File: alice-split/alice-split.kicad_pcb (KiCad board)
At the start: 2 copper layers, 434.2 x 120 mm, 214 parts, among them J1 MJ-4PP-9-Lily58-cache-Lily58_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, J2 OLED-Lily58-cache, J3 OLED-Lily58-cache, J4 MJ-4PP-9-Lily58-cache-Lily58_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, SW38 SW_PUSH-MX_W_LED, SW39 SW_PUSH-MX_W_LED, SW40 SW_PUSH-MX_W_LED, SW41 SW_PUSH-MX_W_LED, SW42 SW_PUSH-MX_W_LED, SW43 SW_PUSH-MX_W_LED, SW44 SW_PUSH-MX_W_LED, SW45 SW_PUSH-MX_W_LED, SW46 SW_PUSH-MX_W_LED, SW47 SW_PUSH-MX_W_LED, SW48 SW_PUSH-MX_W_LED, SW49 SW_PUSH-MX_W_LED, SW50 SW_PUSH-MX_W_LED, SW51 SW_PUSH-MX_W_LED, SW52 SW_PUSH-MX_W_LED, SW53 SW_PUSH-MX_W_LED, SW54 SW_PUSH-MX_W_LED, SW55 SW_PUSH-MX_W_LED, SW56 SW_PUSH-MX_W_LED, SW57 SW_PUSH-MX_W_LED, SW58 SW_PUSH-MX_W_LED, SW59 SW_PUSH-MX_W_LED, SW60 SW_PUSH-MX_W_LED, SW61 SW_PUSH-MX_W_LED, SW62 SW_PUSH-MX_W_LED, SW63 SW_PUSH-MX_W_LED, SW64 SW_PUSH-MX_W_LED, SW65 SW_PUSH-MX_W_LED, SW66 SW_PUSH-MX_W_LED, SW67 SW_PUSH-MX_W_LED, SW68 SW_PUSH-MX_W_LED, SW69 SW_PUSH-MX_W_LED, SW70 SW_PUSH-MX_W_LED, SW71 SW_PUSH-MX_W_LED, SW72 SW_PUSH-MX_W_LED, SW73 SW_PUSH-MX_W_LED, SW74 SW_PUSH-MX_W_LED, SW75 SW_PUSH-MX_W_LED, SW76 SW_PUSH-MX_W_LED, SW77 SW_PUSH-MX_W_LED, SW78 SW_PUSH-MX_W_LED, SW79 SW_PUSH-MX_W_LED, SW80 SW_PUSH-MX_W_LED, SW81 SW_PUSH-MX_W_LED, SW82 SW_PUSH-MX_W_LED, SW83 SW_PUSH-MX_W_LED, SW84 SW_PUSH-MX_W_LED, SW85 SW_PUSH-MX_W_LED, SW86 SW_PUSH-MX_W_LED, SW87 SW_PUSH-MX_W_LED, SW88 SW_PUSH-MX_W_LED, SW89 SW_PUSH-MX_W_LED, U1 Sparkfun_Pro_Micro, U2 ProMicro_2-Lily58-cache-Lily5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

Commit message: Working on making the outer profiles of the PCBs more consistent with each other design wise.
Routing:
- net GND: track 2924.6 -> 2939.3 mm
- net /Right Hand Side/COL0: track 281.2 -> 282.0 mm
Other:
- outline, holes or cut-outs redrawn

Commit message: Started trying to re-arrange the left hand side macro keys.
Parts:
- added D40: D_Small, Diode_SMD:D_1206_3216Metric, B.Cu at (49.2, 134.5)
- added D74: D_Small, Diode_SMD:D_1206_3216Metric, B.Cu at (48.5, 111.5)
- added R3: R_Small, SofleKeyboard-footprint:R_1206_DoubleSided, F.Cu at (292.1, 68.5)
- added R4: R_Small, SofleKeyboard-footprint:R_1206_DoubleSided, F.Cu at (292.1, 71.8)
- added SW_MACRO3: SW_PUSH-MX_W_LED, SofleRGB:SK6812MINI_and_cherry, F.Cu at (56.5, 109.9)
- added SW_MACRO4: SW_PUSH-MX_W_LED, SofleRGB:SK6812MINI_and_cherry, F.Cu at (463.7, 124.8)
- moved SW_MACRO2 406.6 mm to (57.1, 132.9)
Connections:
- SW_MACRO2 pad 1: Net-(SW_MACRO2B-DOUT) -> unconnected-(SW_MACRO2B-DOUT-Pad1)
- SW_MACRO2 pad 2: /Right Hand Side/VCC -> unconnected-(SW_MACRO2B-VSS-Pad2)
- SW_MACRO2 pad 3: Net-(D_ENC_R1-DOUT) -> unconnected-(SW_MACRO2B-DIN-Pad3)
- SW_MACRO2 pad 4: GND -> unconnected-(SW_MACRO2B-VDD-Pad4)
- SW_MACRO2 pad 5: Net-(D73-A) -> Net-(D40-A)
- SW_MACRO2 pad 6: /Right Hand Side/COL1 -> /COL6
- SW_MOD_R1 pad 3: Net-(SW_MACRO2B-DOUT) -> Net-(SW_MACRO4B-DOUT)
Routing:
- net Net-(SW_MACRO4B-DOUT): track 0.00 -> 89.0 mm
- net Net-(SW_MACRO2B-DOUT): track 89.0 -> 0.00 mm
- net /ROW2: track 234.6 -> 224.5 mm
- net /ROW1: track 246.8 -> 237.7 mm
- net Net-(SW_MACRO1B-DOUT): track 162.7 -> 160.3 mm
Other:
- board size 434.2 x 120 mm -> 434.2 x 119.2 mm

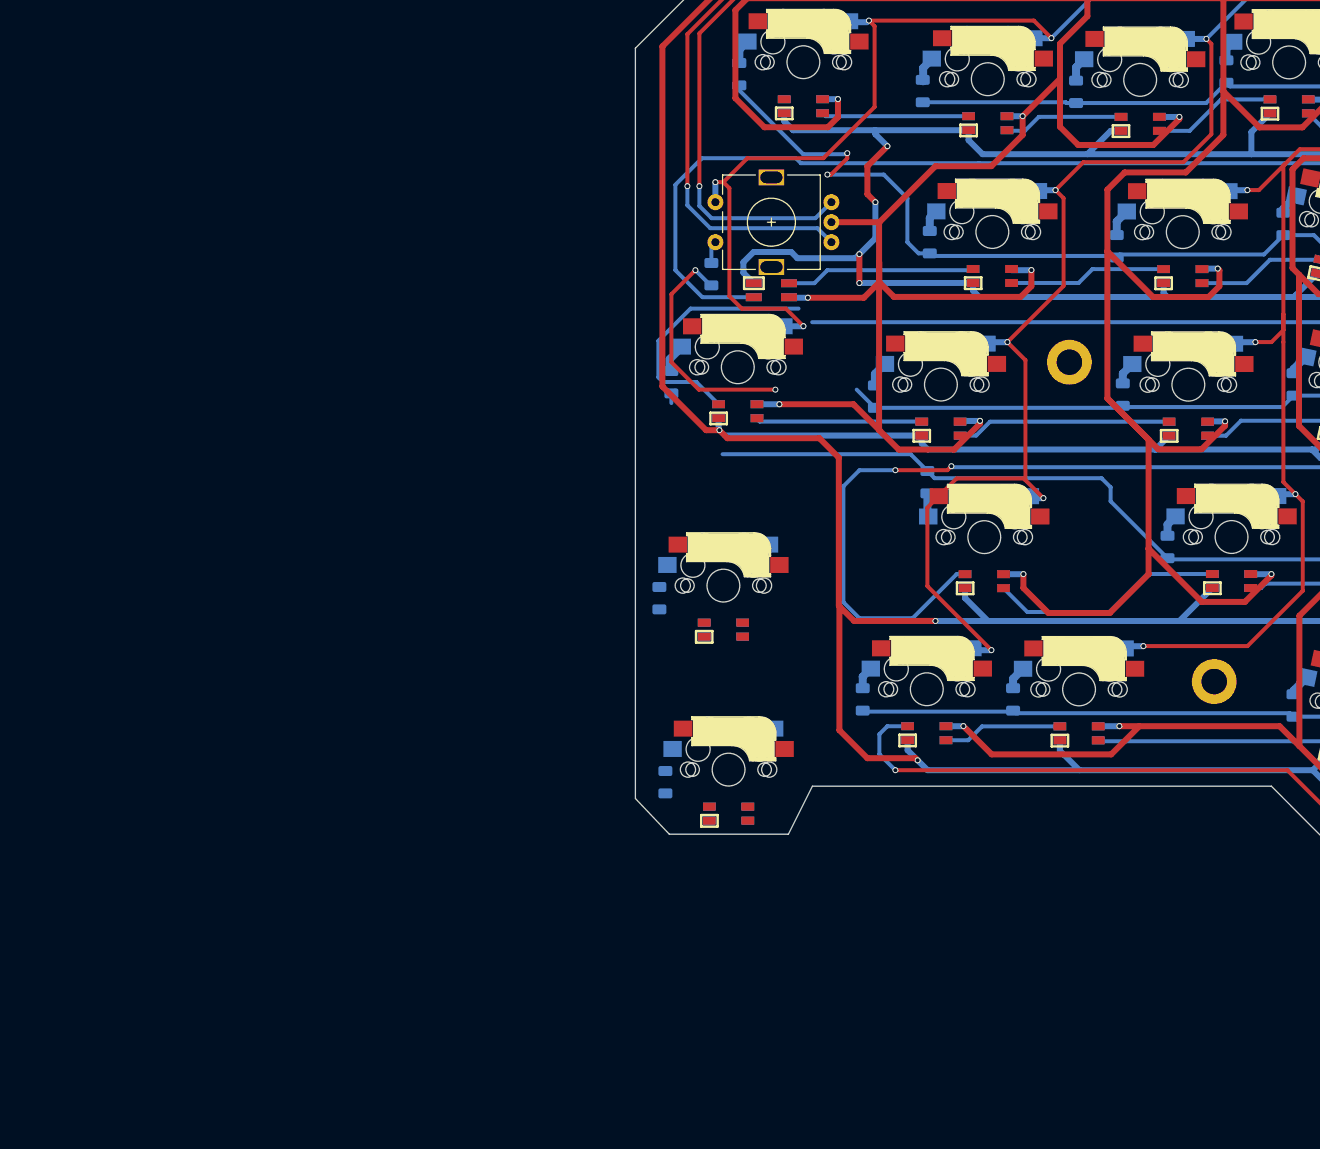
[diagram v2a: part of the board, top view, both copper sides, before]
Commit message: Working on adding more macro keys to the left hand side.
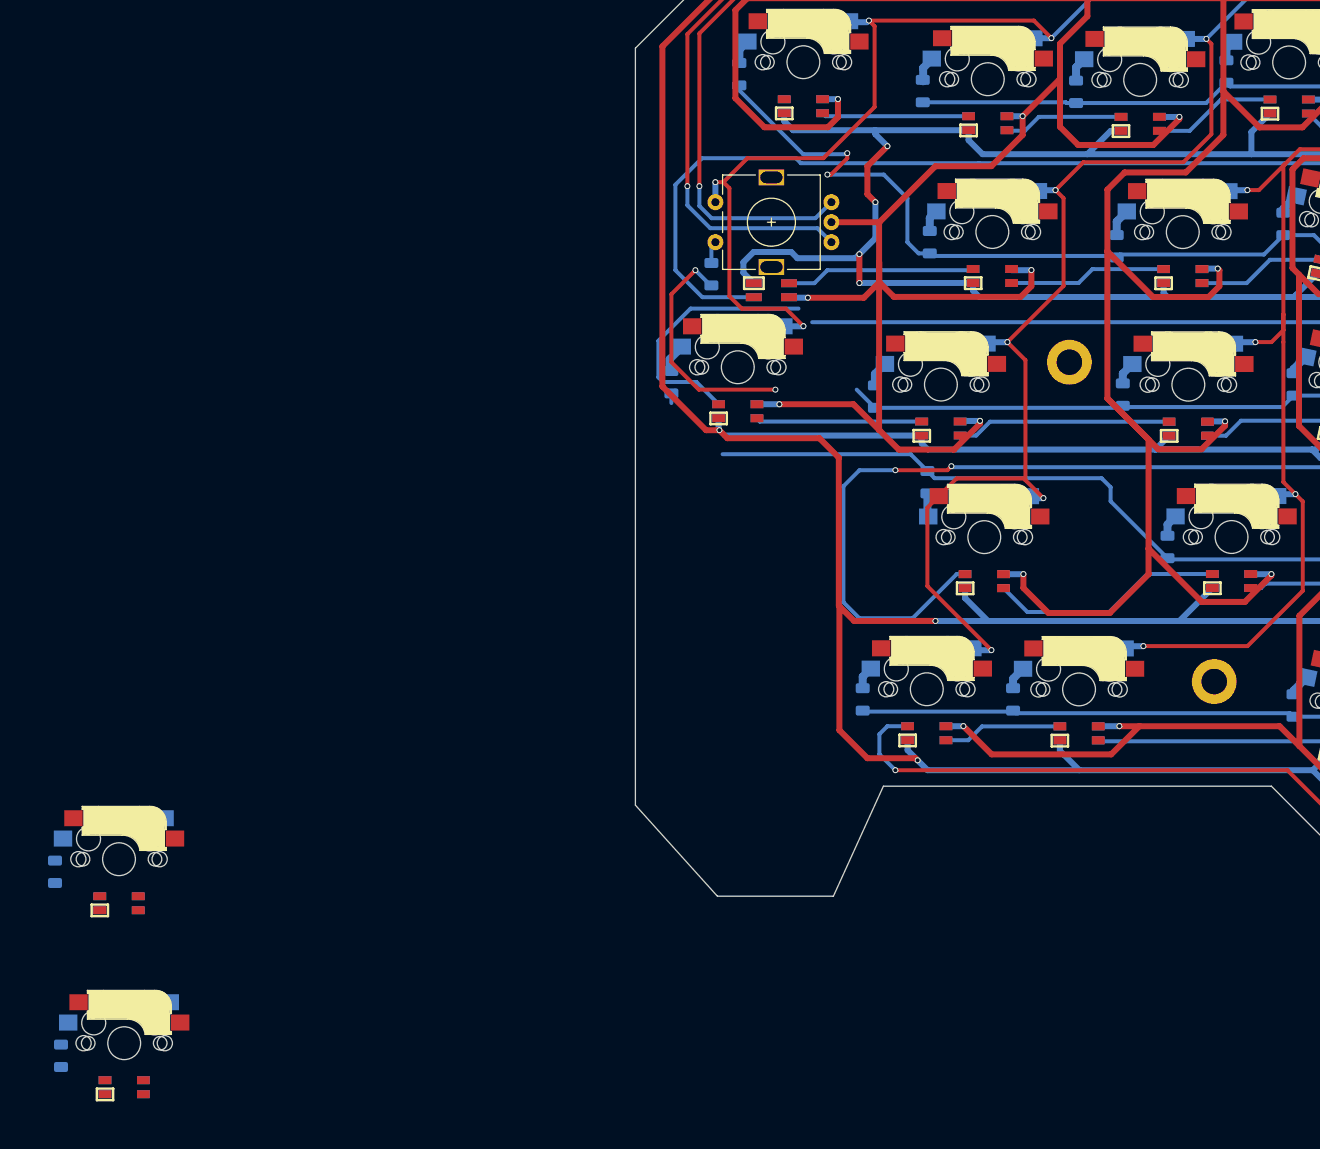
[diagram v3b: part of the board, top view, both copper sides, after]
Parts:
- moved SW_MACRO3 82.9 mm to (-19.1, 144.1)
- moved D40 82.9 mm to (-26.3, 168.7)
- moved D74 82.9 mm to (-27.1, 145.7)
- moved SW_MACRO2 82.9 mm to (-18.4, 167.1)
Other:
- outline, holes or cut-outs redrawn
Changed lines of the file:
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@@
 	(footprint "SofleRGB:SK6812MINI_and_cherry"
 		(layer "F.Cu")
-		(at 56.5 109.92625)
+		(at -19.05 144.125)
 		(property "Reference" "SW_MACRO3"
 			(at 0 3 180)
@@
 	(footprint "SofleRGB:SK6812MINI_and_cherry"
 		(layer "F.Cu")
-		(at 57.15 132.92625)
+		(at -18.4 167.125)
 		(property "Reference" "SW_MACRO2"
 			(at 0 3 180)
@@
 	(footprint "Diode_SMD:D_1206_3216Metric"
 		(layer "B.Cu")
-		(at 48.5 111.5 90)
+		(at -27.05 145.69875 90)
 		(descr "Diode SMD 1206 (3216 Metric), square (rectangular) end terminal, IPC-7351 nominal, (Body size source: http://www.tortai-tech.com/upload/download/2011102023233369053.pdf), generated with kicad-footprint-generator")
 		(tags "diode")
@@
 	(footprint "Diode_SMD:D_1206_3216Metric"
 		(layer "B.Cu")
-		(at 49.25 134.5 90)
+		(at -26.3 168.69875 90)
 		(descr "Diode SMD 1206 (3216 Metric), square (rectangular) end terminal, IPC-7351 nominal, (Body size source: http://www.tortai-tech.com/upload/download/2011102023233369053.pdf), generated with kicad-footprint-generator")
 		(tags "diode")
@@
 		)
 		(property "Sim.Device" "D"
-			(at 0 0 -90)
+			(at 0 0 270)
 			(unlocked yes)
 			(layer "B.Fab")
@@
 		)
 		(property "Sim.Pins" "1=K 2=A"
-			(at 0 0 -90)
+			(at 0 0 270)
 			(unlocked yes)
 			(layer "B.Fab")
@@
 		(layer "Dwgs.User")
 	)
+	(gr_rect
+		(start 449.06 79.72267)
+		(end 463.049175 93.69839)
+		(stroke
+			(width 0.1)
+			(type default)
+		)
+		(fill no)
+		(layer "Dwgs.User")
+	)
 	(gr_arc
 		(start 353.127097 60.77502)
@@
 		(layer "Dwgs.User")
 	)
+	(gr_rect
+		(start 444.000578 98.681451)
+		(end 457.989753 112.657171)
+		(stroke
+			(width 0.1)
+			(type default)
+		)
+		(fill no)
+		(layer "Dwgs.User")
+	)
 	(gr_arc
 		(start 372.105503 102.896522)
@@
 		(layer "Dwgs.User")
 	)
+	(gr_rect
+		(start 443.531173 41.574487)
+		(end 457.520348 55.550207)
+		(stroke
+			(width 0.1)
+			(type default)
+		)
+		(fill no)
+		(layer "Dwgs.User")
+	)
 	(gr_line
 		(start 176.261863 125.336214)
@@
 		(layer "Dwgs.User")
 	)
+	(gr_rect
+		(start 456.707994 117.851862)
+		(end 470.697169 131.827582)
+		(stroke
+			(width 0.1)
+			(type default)
+		)
+		(fill no)
+		(layer "Dwgs.User")
+	)
 	(gr_line
 		(start 322.334597 92.98259)
@@
 		(layer "Dwgs.User")
 	)
+	(gr_rect
+		(start 451.94 60.67962)
+		(end 465.929175 74.65534)
+		(stroke
+			(width 0.1)
+			(type default)
+		)
+		(fill no)
+		(layer "Dwgs.User")
+	)
 	(gr_arc
 		(start 193.621475 130.048439)
@@
 			(xy 225.25 30.25) (xy 225.25 98.25) (xy 212.75 110.75) (xy 212.75 126) (xy 212.75 144.75) (xy 208 149.5)
 			(xy 190 149.5) (xy 186.5 146) (xy 168.5 146) (xy 166.004353 143.5) (xy 133.542662 143.576584) (xy 125 135)
-			(xy 67.625 135) (xy 64.625 141) (xy 49.737494 141) (xy 45.5 136.539483) (xy 45.5 42.75) (xy 58 30.25)
+			(xy 76.5 135) (xy 70.25 148.75) (xy 55.75 148.75) (xy 45.5 137.36844) (xy 45.5 42.75) (xy 58 30.25)
 		)
 		(stroke
@@
 		(layer "F.CrtYd")
 	)
+	(gr_rect
+		(start -33.328592 39.984765)
+		(end -47.317767 53.960485)
+		(stroke
+			(width 0.1)
+			(type default)
+		)
+		(fill no)
+		(layer "User.2")
+	)
+	(gr_rect
+		(start 61.994587 95)
+		(end 48.005412 108.97572)
+		(stroke
+			(width 0.1)
+			(type default)
+		)
+		(fill no)
+		(layer "User.2")
+	)
+	(gr_rect
+		(start 64.874587 114.04305)
+		(end 50.885412 128.01877)
+		(stroke
+			(width 0.1)
+			(type default)
+		)
+		(fill no)
+		(layer "User.2")
+	)
+	(gr_rect
+		(start 69.934009 133.001831)
+		(end 55.944834 146.977551)
+		(stroke
+			(width 0.1)
+			(type default)
+		)
+		(fill no)
+		(layer "User.2")
+	)
 	(segment
